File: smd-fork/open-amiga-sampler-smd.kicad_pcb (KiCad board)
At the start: 2 copper layers, 36.3 x 27 mm, 17 parts, among them J1 Left, J2 Right, J3 DB25_Male, U1 ADC0820CCN, U2 MCP6001U

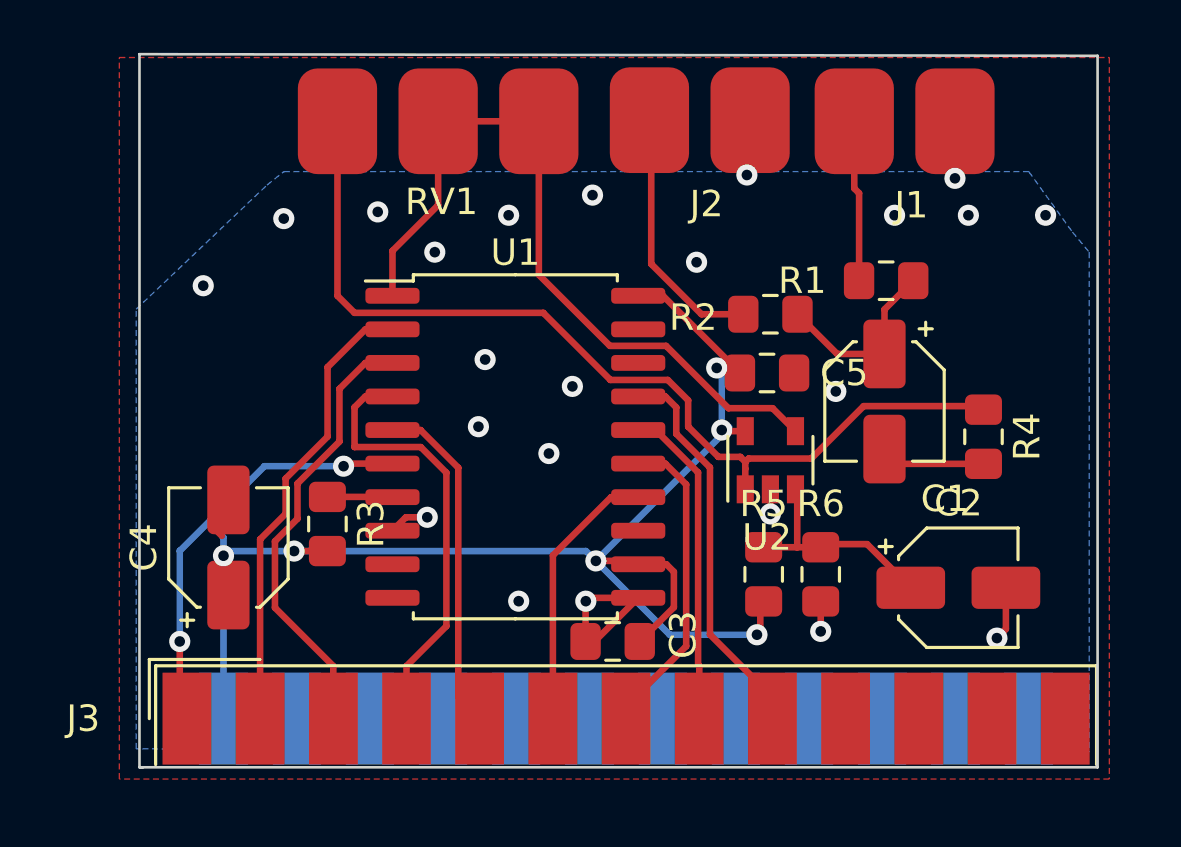
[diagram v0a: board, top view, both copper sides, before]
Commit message: tidied up positions and silkscreen
Added new nilkscreen items and adjusted positions of a few components to avoid courtyard violations in DRC. upgraded VCC trace to be thicker
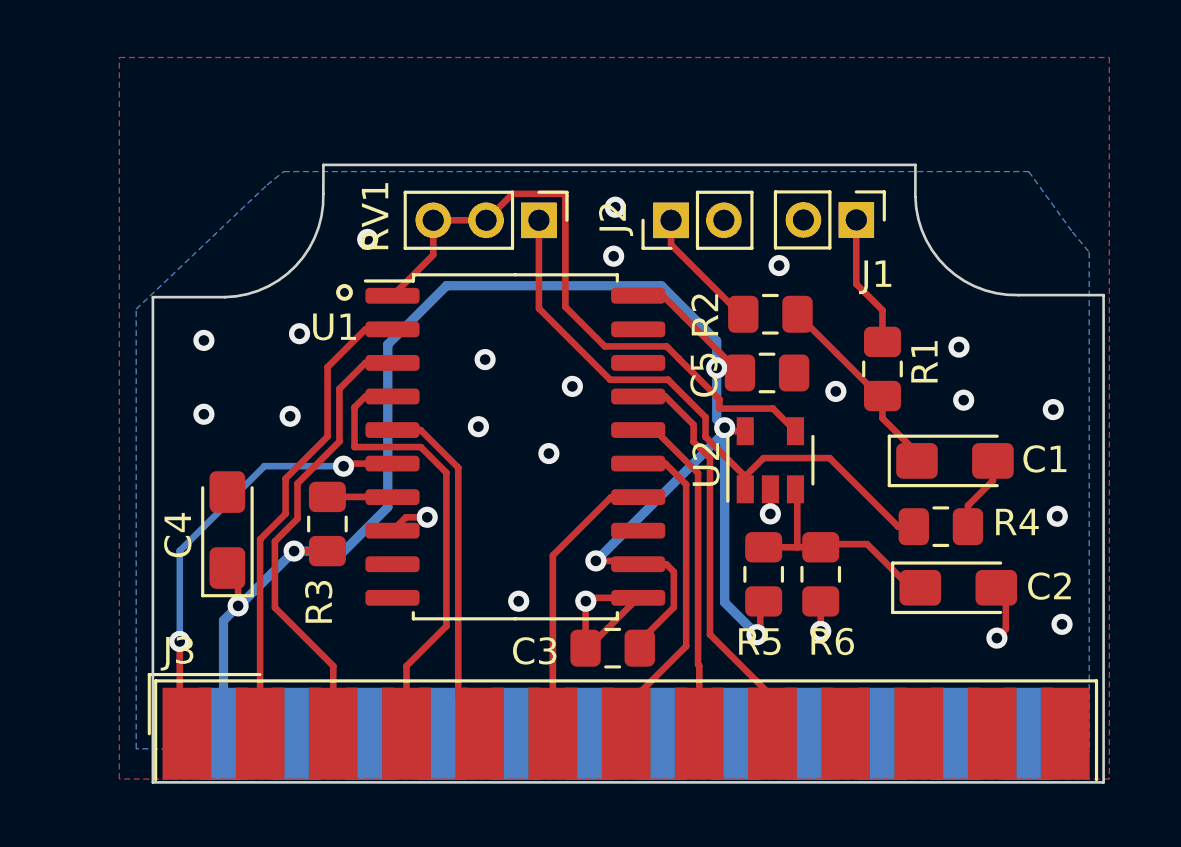
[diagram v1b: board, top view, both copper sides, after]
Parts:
- added REF**: OSHW-Logo2_9.8x8mm_SilkScreen, Symbol:OSHW-Logo2_9.8x8mm_SilkScreen, B.Cu at (88.8, 143.7)
- C1, C2, C4: footprint Capacitor_SMD:CP_Elec_4x4.5 -> Capacitor_Tantalum_SMD:CP_EIA-3216-18_Kemet-A_Pad1.58x1.35mm_HandSolder
- J1, J2: footprint connectors:Audio pads -> Connector_PinHeader_2.00mm:PinHeader_1x02_P2.00mm_Vertical
- RV1: footprint connectors:Pot pads -> Connector_PinHeader_2.00mm:PinHeader_1x03_P2.00mm_Vertical
- moved RV1 7.10 mm to (95.0, 131.0), turned to 270 degrees
- moved J1 6.05 mm to (107.0, 131.0), turned to 270 degrees
- moved J2 5.92 mm to (100.0, 131.0), turned to 90 degrees
- moved R4 3.77 mm to (110.2, 142.6), turned to 0 degrees
- moved C1 3.49 mm to (110.7, 140.1), turned to 0 degrees
- moved R1 3.34 mm to (108.0, 136.6), turned to 90 degrees
- moved C4 0.66 mm to (83.2, 142.7)
- moved J3 0.57 mm to (98.3, 150.4)
- moved C3 0.25 mm to (97.8, 147.2)
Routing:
- net Net-(R4-Pad1): track 36.2 -> 22.9 mm
- net VCC: track 55.7 -> 68.9 mm
- net Net-(J2-Pad1): track 10.1 -> 4.75 mm
- net Vo: track 29.1 -> 24.0 mm
- net GND: track 16.6 -> 11.9 mm, vias 23 -> 24
- net Net-(C1-Pad2): track 3.98 -> 2.88 mm
- net Net-(J1-Pad1): track 6.11 -> 5.03 mm
- net MONO_AUDIO: track 8.32 -> 7.49 mm
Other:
- board size 36.3 x 27 mm -> 36 x 23.4 mm
- net class pwr added: clearance 0.2, trace_width 0.35, via_dia 0.8, via_drill 0.4
- board text added: "L GND R"
- board text added: "Open Amiga Sampler @echolevel @mnstrmnch @abrugsch"
- board text added: "POT"

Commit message: VCC improvements
changed mailn bulk bypass cap to electrolytic. moved C3 to close to U1 Vcc. tweaked Vcc traces for better path. Silkscreen++
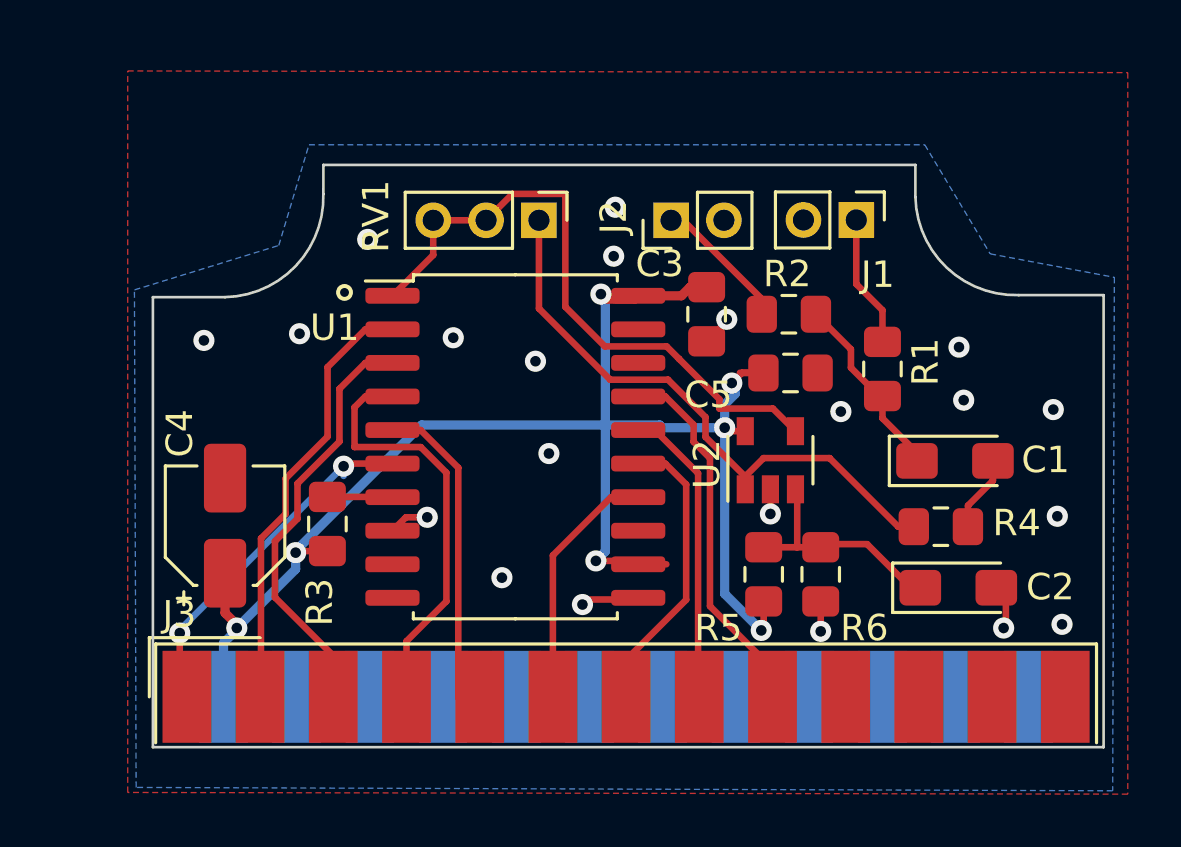
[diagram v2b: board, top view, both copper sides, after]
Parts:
- C4: footprint Capacitor_Tantalum_SMD:CP_EIA-3216-18_Kemet-A_Pad1.58x1.35mm_HandSolder -> Capacitor_SMD:CP_Elec_4x5.3
- moved C3 13.1 mm to (101.3, 134.6), turned to 270 degrees
- moved REF** 3.66 mm to (85.2, 143.1)
- moved J3 1.40 mm to (98.3, 149.0)
- moved C5 0.89 mm to (104.5, 136.8)
- moved R2 0.70 mm to (104.5, 134.6)
- moved C4 0.19 mm to (83.1, 142.6)
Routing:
- net VCC: track 68.9 -> 61.9 mm, vias 6 -> 7
- net GND: track 11.9 -> 8.52 mm, vias 24 -> 21
- net STROBE: track 15.9 -> 14.6 mm
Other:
- board size 36 x 23.4 mm -> 36 x 22 mm

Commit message: fixed unconnected grounds
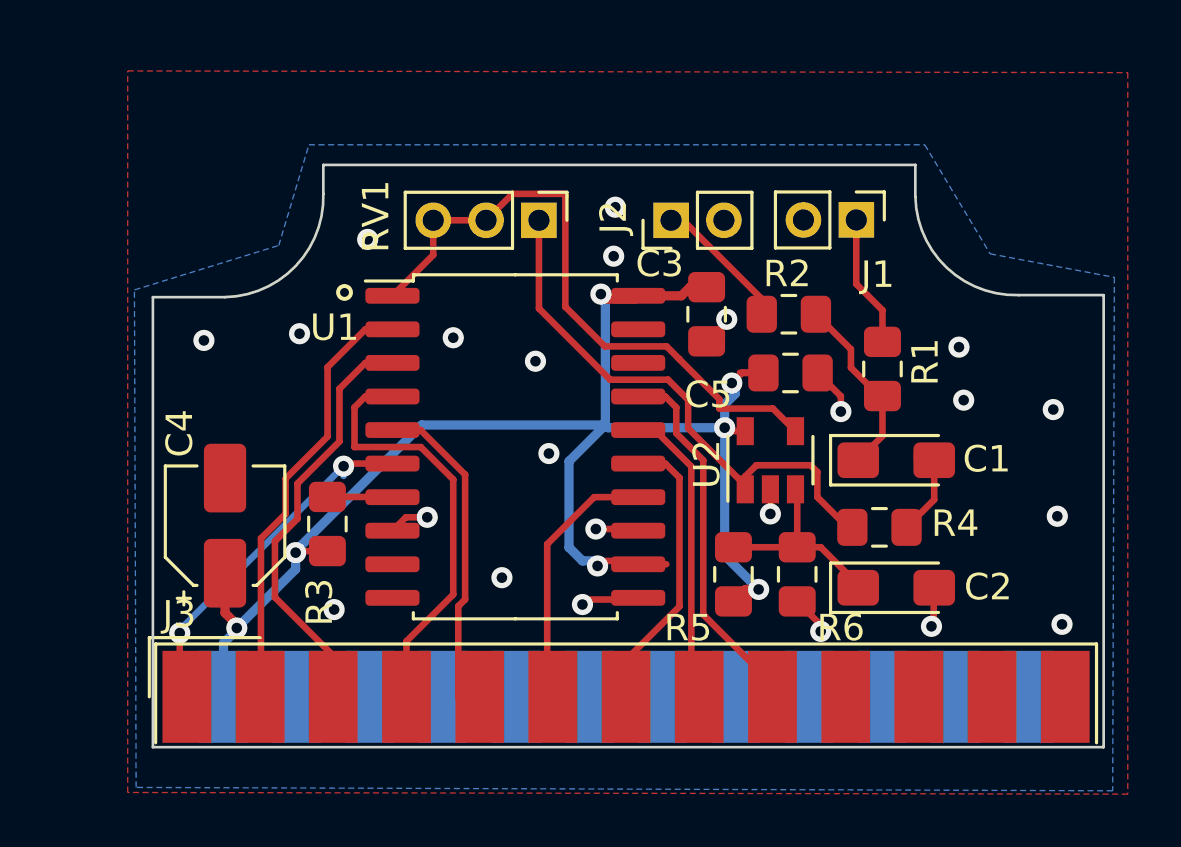
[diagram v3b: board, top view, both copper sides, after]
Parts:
- moved C2 2.35 mm to (108.5, 144.9)
- moved R4 2.32 mm to (107.9, 142.6)
- moved C1 2.22 mm to (108.5, 140.1)
- moved R5 1.14 mm to (102.4, 144.4)
- moved R6 0.89 mm to (104.8, 144.4)
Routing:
- net GND: track 8.52 -> 12.3 mm, vias 21 -> 23
- net Net-(R4-Pad1): track 22.9 -> 20.9 mm
- net Net-(C2-Pad1): track 8.63 -> 7.62 mm
- net Net-(C1-Pad2): track 2.88 -> 3.87 mm
- net D4: track 10.3 -> 10.9 mm
